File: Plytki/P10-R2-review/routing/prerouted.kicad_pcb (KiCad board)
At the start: 2 copper layers, 53 x 100 mm, 24 parts, among them J1 J_BP, J2 SERWIS, J3 OBD, U1 TCAN1051V, U2 74LVC125AD

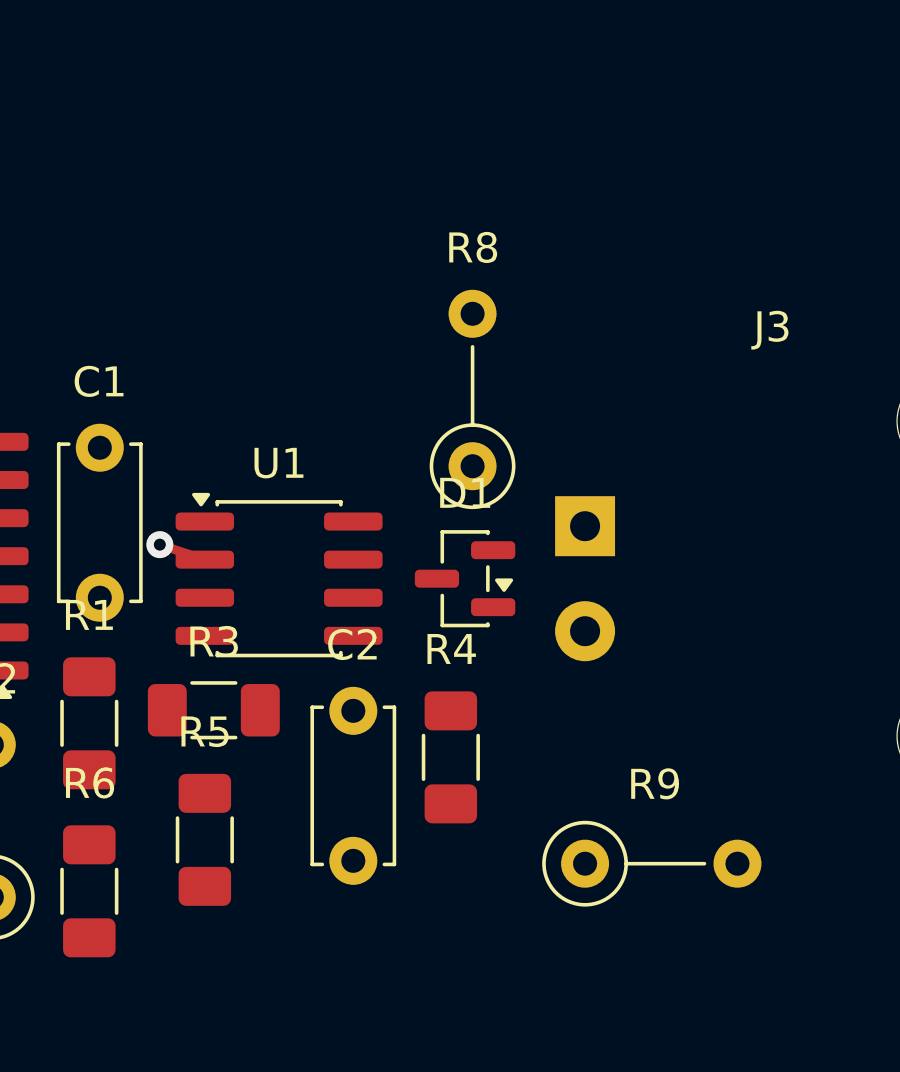
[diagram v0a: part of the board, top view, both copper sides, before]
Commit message: P10 R2 PCB: poprawki po recenzji (CAN przez D1, pierścień wokół J3, nadruk, kontrole)
- CAN_H / CAN_L zablokowane z J3 przez pola D1 do U1 (było: CAN_H do D1
  odgałęzieniem 3 mm); obejście D1 1,4 mm zostawia miejsce na przelotkę
  GND D1.3; korytarz linii wolny przy rozmieszczaniu
- pierścień 1 mm bez innej miedzi wokół lutowanych pól J3 (F.Cu z kanałem
  dla linii do D1, B.Cu pełny); było SRV_CAN_TX 0,26 mm od pól
- nadruk: oznaczenie zawsze bliżej swojej części, tytuł ze slotem
  (S1 §9), „H”/„L” przy polach J3; ukryte oznaczenia na rysunku z F.Fab
- kontrole: przez D1, odstęp od pól J3, pas A (S1 §5), najbliższy obrys,
  znaczniki, etykiety z tabeli LABEL; próby ujemne 24/24 (+6)
- PDF: podpis renderu bez modeli 3D, liczebniki, stopka; teksty ZAKUPY,
  QA, README, WIAZKI (punkt widzenia „po prawej”)
- DRC 0/0/0, kontrole PCB 24/24

Co-Authored-By: Claude Opus 5.5 <noreply@anthropic.com>
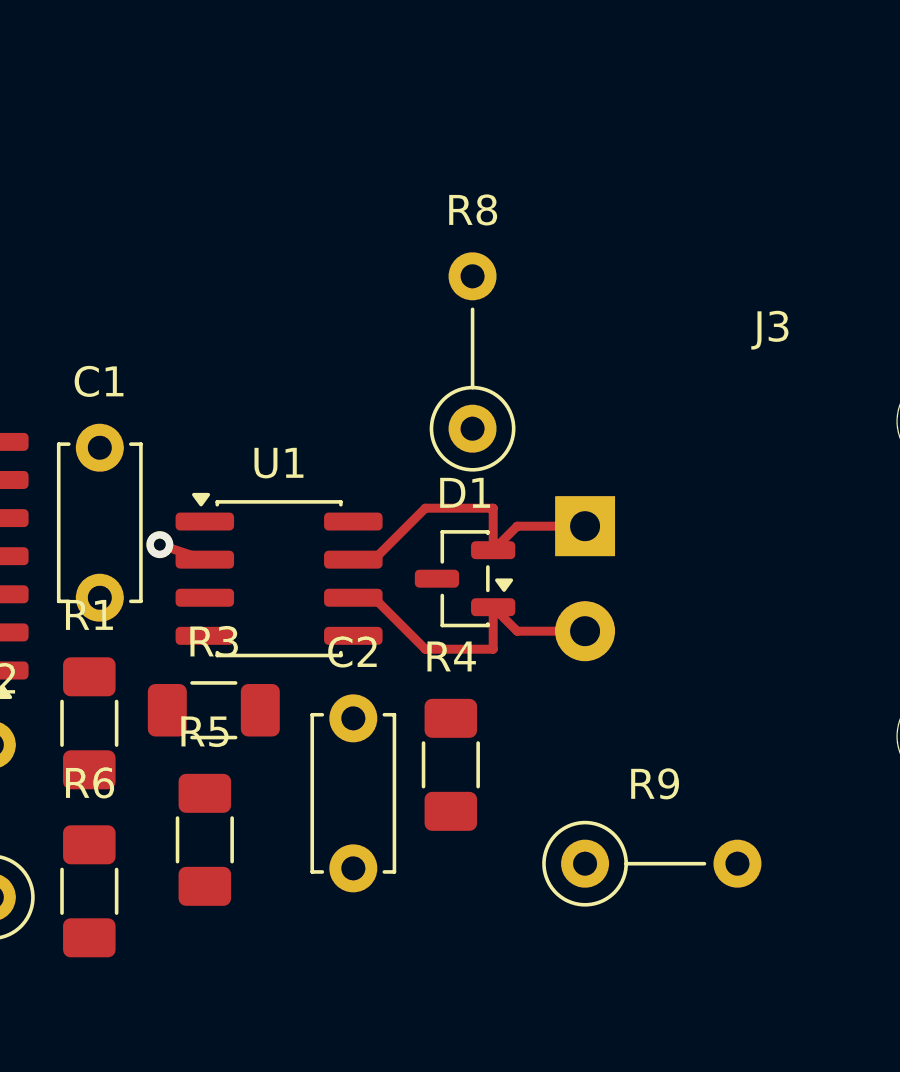
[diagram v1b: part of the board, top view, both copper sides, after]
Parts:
- moved R8 1.25 mm to (31.2, 51.8)
- moved C2 0.25 mm to (27.3, 61.4)
- moved R4 0.25 mm to (30.5, 63.0)
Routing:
- net CAN_L: track 0.00 -> 10.2 mm
- net CAN_H: track 0.00 -> 10.2 mm
